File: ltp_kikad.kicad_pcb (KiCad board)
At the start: 2 copper layers, 65 x 56.5 mm, 71 parts, among them IC1 SamacSys_Parts_HT16K33-28SOP, IC2 SamacSys_Parts_HT16K33-28SOP, J1 SM04B-SRSS-TB(LF)(SN), J2 RPi_GPIO, U1 MCP2515-xSO, U2 MCP2551-I-SN, U3 PCA9306DP, Y1 16MHz

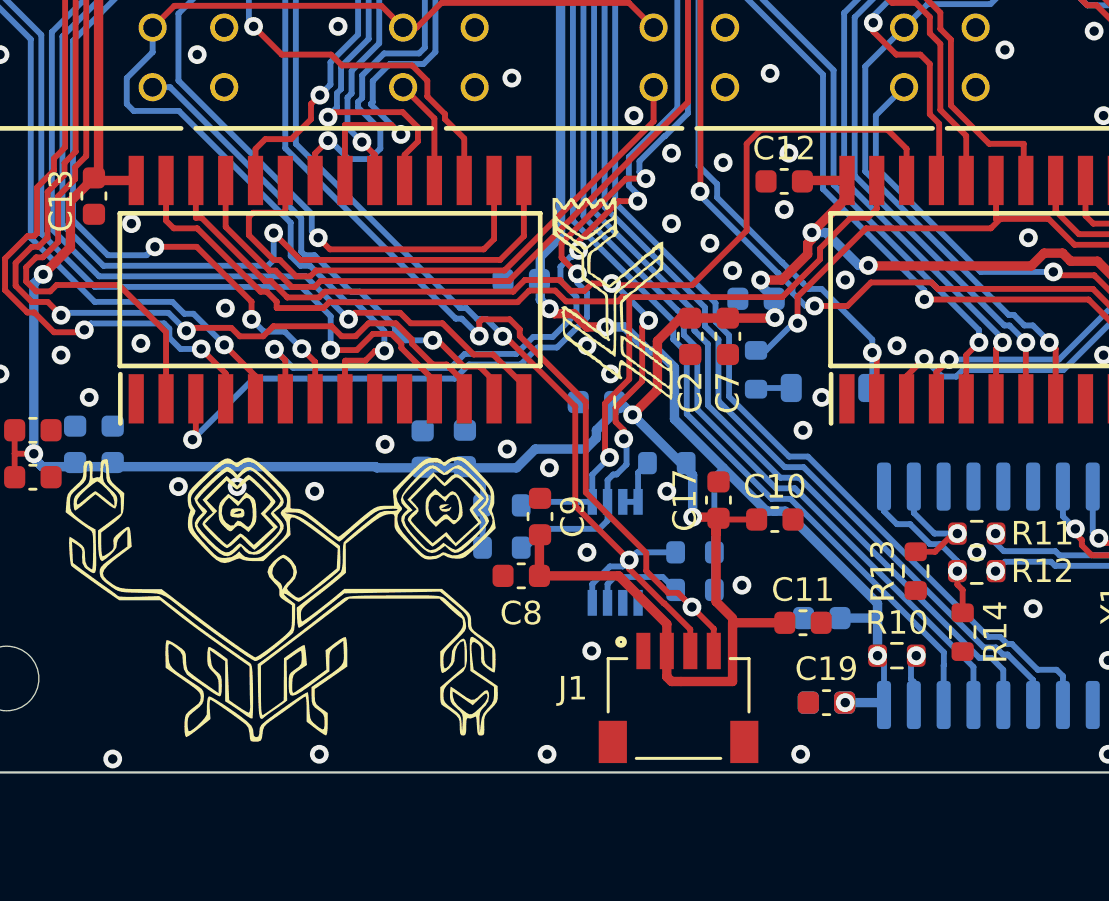
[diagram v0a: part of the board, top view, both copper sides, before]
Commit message: Add testpoints
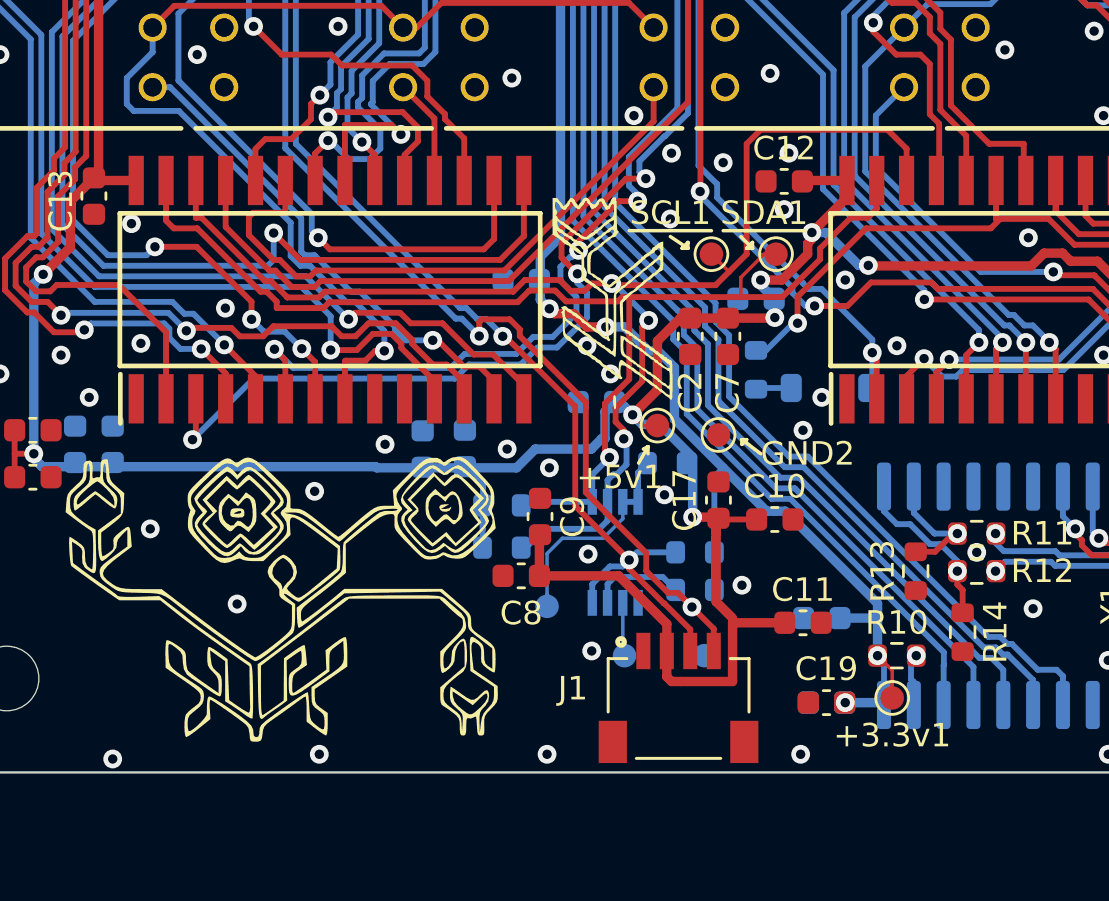
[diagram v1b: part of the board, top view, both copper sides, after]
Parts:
- added +3.3V2: TP3.3v, TestPoint:TestPoint_Pad_D1.0mm, B.Cu at (148.8, 104.6)
- added +3.3v1: TestPoint, TestPoint:TestPoint_Pad_D1.0mm, F.Cu at (160.2, 106.4)
- added +5v1: TestPoint, TestPoint:TestPoint_Pad_D1.0mm, F.Cu at (150.2, 94.8)
- added GND1: TestPoint, TestPoint:TestPoint_Pad_D1.0mm, B.Cu at (152.2, 104.6)
- added GND2: TestPoint, TestPoint:TestPoint_Pad_D1.0mm, F.Cu at (152.8, 95.2)
- added SCL1: SCL, TestPoint:TestPoint_Pad_D1.0mm, F.Cu at (152.5, 87.5)
- added SDA1: SDA, TestPoint:TestPoint_Pad_D1.0mm, F.Cu at (155.2, 87.5)
- added Vfref2: Vref2, TestPoint:TestPoint_Pad_D1.0mm, B.Cu at (145.5, 102.5)
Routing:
- net Net-(U3-EN): track 2.47 -> 9.12 mm
- net SDA: track 49.9 -> 52.7 mm
- net +3V3: track 0.00 -> 2.18 mm
- net +3.3V: track 88.3 -> 90.4 mm
- net +5V: track 177.5 -> 179.4 mm
- net SCL: track 56.7 -> 58.3 mm
- net GND: vias 101 -> 99

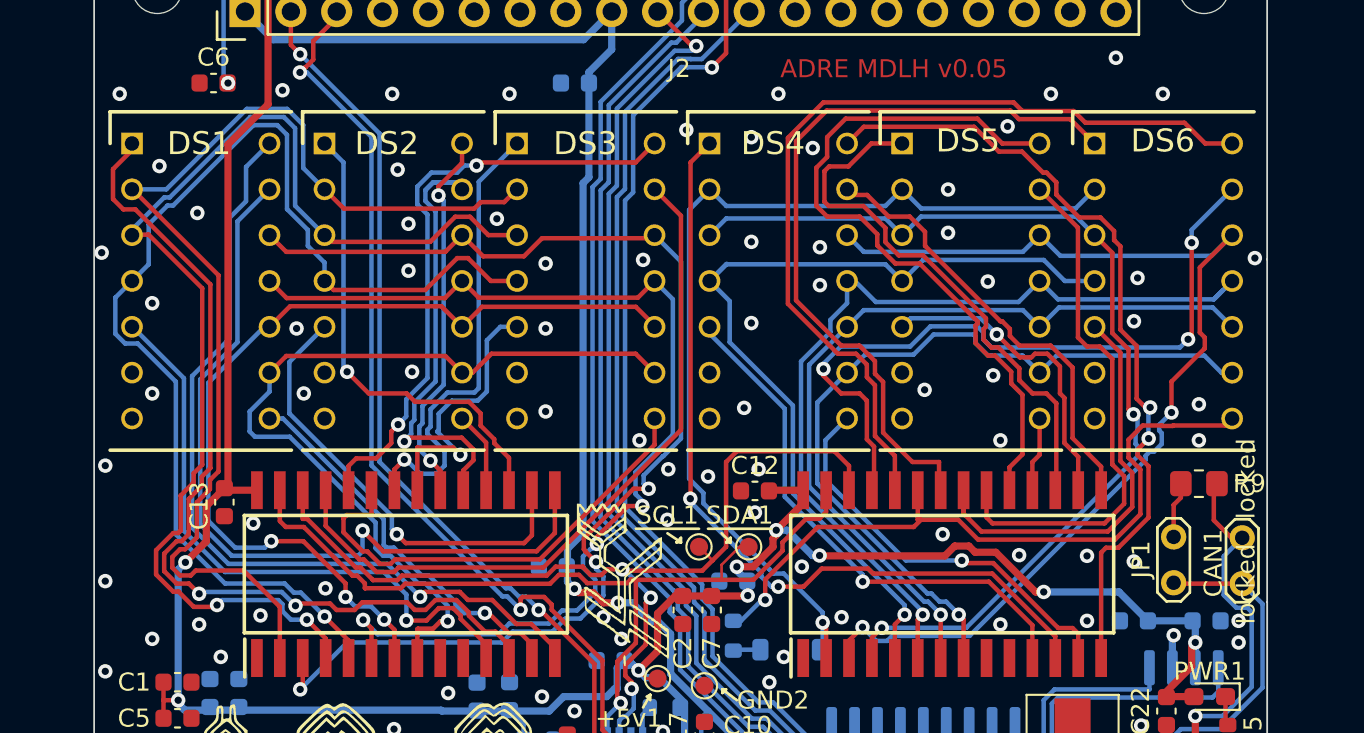
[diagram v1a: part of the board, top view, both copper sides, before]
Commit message: Minimize distances between displays
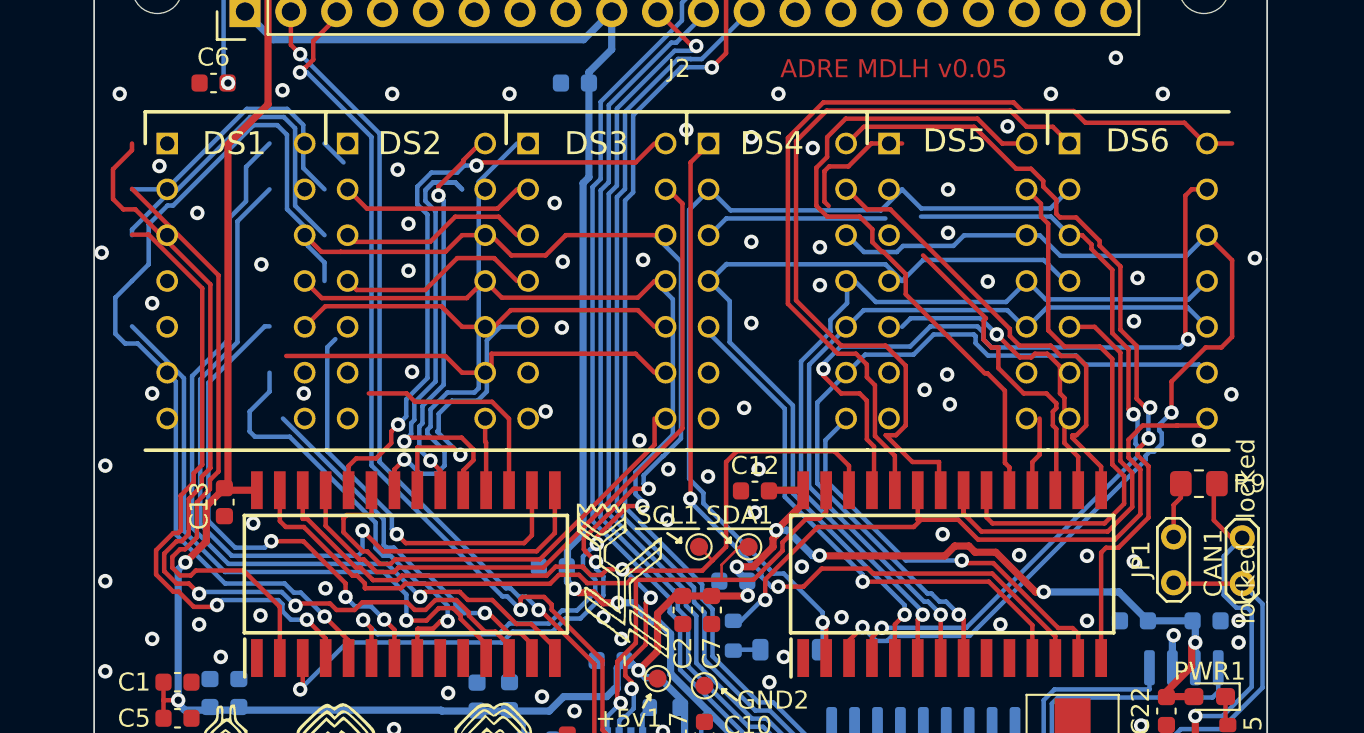
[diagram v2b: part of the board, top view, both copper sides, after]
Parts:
- moved DS1 1.95 mm to (123.0, 65.2)
- moved DS6 1.39 mm to (173.0, 65.2)
- moved DS2 1.28 mm to (133.0, 65.2)
- moved DS5 0.72 mm to (163.0, 65.2)
- moved DS3 0.61 mm to (143.0, 65.1)
- moved DS4 0.05 mm to (153.0, 65.1)
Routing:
- net an8: track 26.4 -> 13.8 mm, vias 1 -> 0
- net 2_an8: track 30.7 -> 24.3 mm
- net 2_ca2: track 56.0 -> 53.1 mm
- net 2_an6: track 39.8 -> 37.5 mm
- net 2_ca6: track 44.3 -> 42.1 mm
- net an9: track 25.1 -> 23.0 mm
- net ca5: track 50.7 -> 48.6 mm
- net 2_ca4: track 49.0 -> 47.0 mm
- net ca1: track 67.8 -> 65.8 mm
- net ca4: track 60.2 -> 58.3 mm
- net 2_ca3: track 50.0 -> 48.4 mm
- net 2_an2: track 39.0 -> 37.6 mm
- net 2_an4: track 23.8 -> 25.2 mm
- net 2_ca5: track 45.4 -> 44.1 mm
- net ca0: track 61.4 -> 60.2 mm
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
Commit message: Fix routes
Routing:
- net an8: track 13.8 -> 32.0 mm
- net +5V: track 179.4 -> 172.1 mm, vias 11 -> 10
- net 2_an8: track 24.3 -> 29.2 mm
- net 2_ca2: track 53.1 -> 56.4 mm
- net ca2: track 64.0 -> 61.2 mm
- net an4: track 15.7 -> 18.4 mm
- net ca6: track 45.9 -> 43.8 mm
- net ca3: track 62.7 -> 64.8 mm
- net an10: track 45.0 -> 43.1 mm
- net ca5: track 48.6 -> 46.6 mm
- net 2_ca1: track 59.6 -> 58.0 mm
- net 2_an3: track 42.8 -> 41.2 mm
- net an14: track 34.1 -> 32.5 mm
- net Net-(U1-OSC1): track 11.9 -> 10.3 mm
- net 3.3_SCL: track 64.4 -> 66.0 mm
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
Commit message: Version 0.06
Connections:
- J2 pad 14: unconnected-(J2-GND-Pad14) -> GND
- J2 pad 20: unconnected-(J2-GND-Pad20) -> GND
- J2 pad 25: unconnected-(J2-GND-Pad25) -> GND
- J2 pad 30: unconnected-(J2-GND-Pad30) -> GND
- J2 pad 34: unconnected-(J2-GND-Pad34) -> GND
- J2 pad 9: unconnected-(J2-GND-Pad9) -> GND
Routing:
- net GND: track 5.43 -> 16.5 mm, vias 99 -> 102
- net 2_an6: track 38.3 -> 39.1 mm
- net ca2: track 61.2 -> 61.8 mm
- net ca3: track 64.8 -> 65.4 mm
- net 2_an3: track 41.2 -> 40.6 mm
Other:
- board text added: "MDLH v0.06"
- board text removed: "ADRE MDLH v0.05"

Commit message: Updates
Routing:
- net 2_ca0: track 53.2 -> 53.8 mm
- net GND: vias 102 -> 105

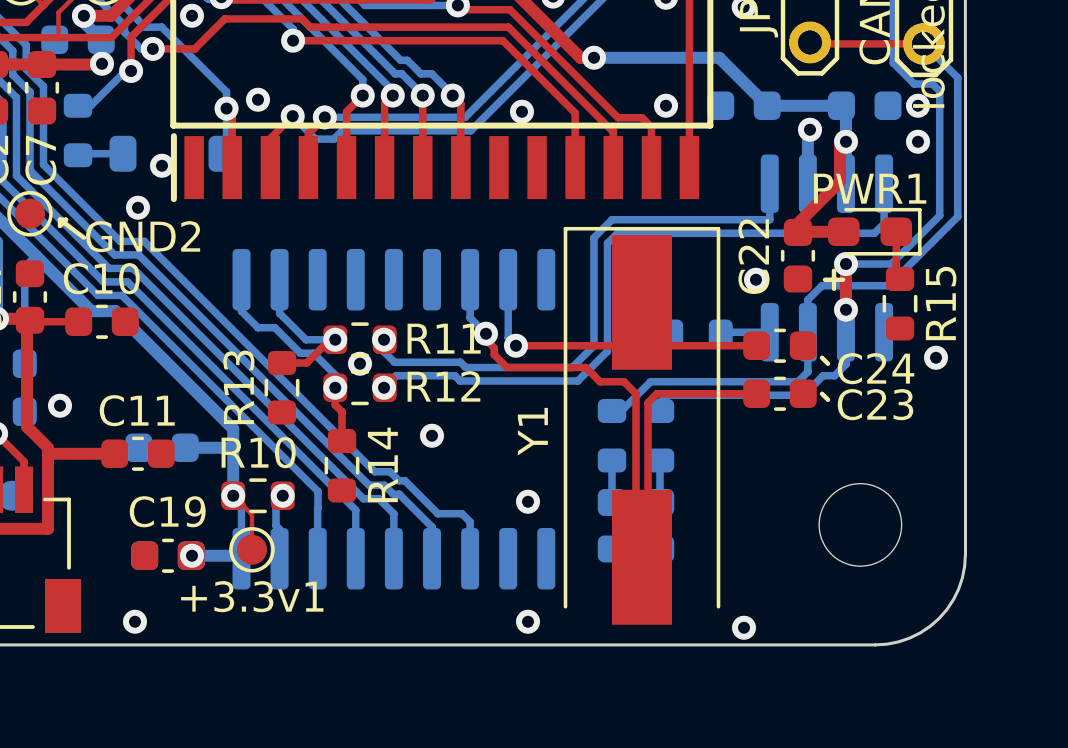
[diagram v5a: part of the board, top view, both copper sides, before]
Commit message: Updates vias
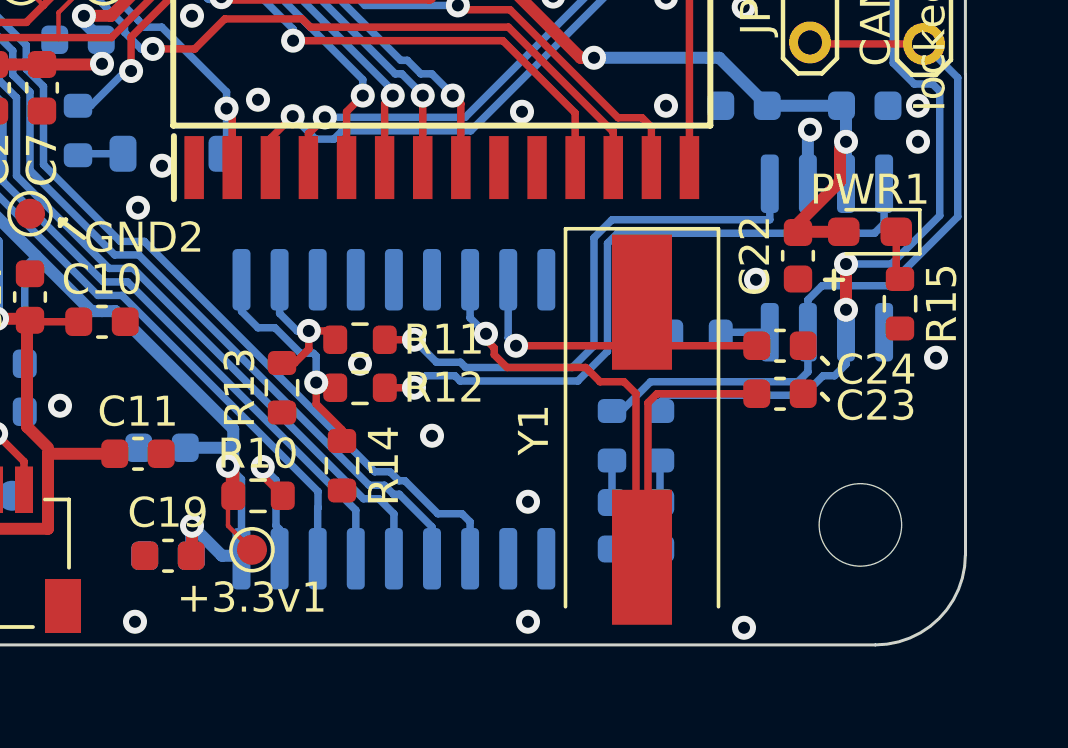
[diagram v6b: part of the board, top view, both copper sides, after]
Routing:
- net +3.3V: track 90.4 -> 95.1 mm
- net Net-(U1-~{RESET}): track 2.24 -> 4.53 mm
- net Net-(U1-TXCAN): track 7.35 -> 8.06 mm
